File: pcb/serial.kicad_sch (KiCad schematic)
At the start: 13 parts, among them J10 SHIELD, J11 DE9_Pins_MountingHoles, J12 01x09, J13 01x09, U94 MAX232

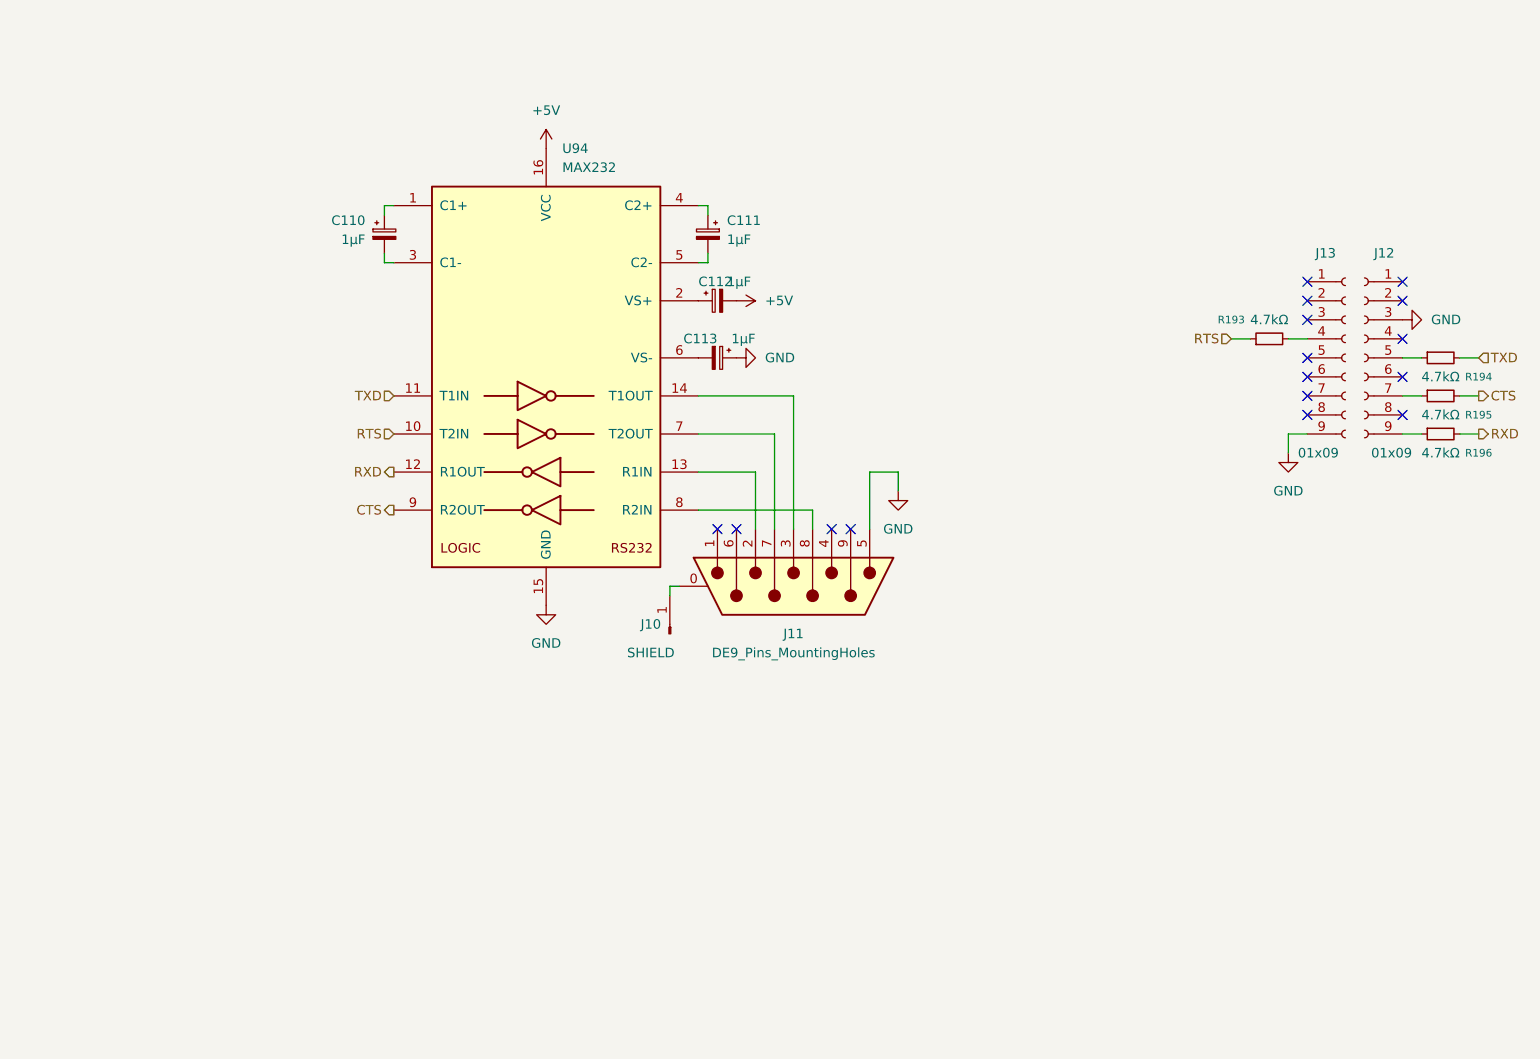
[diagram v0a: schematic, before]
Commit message: WIP PCB (add bypass caps, minor fixes)
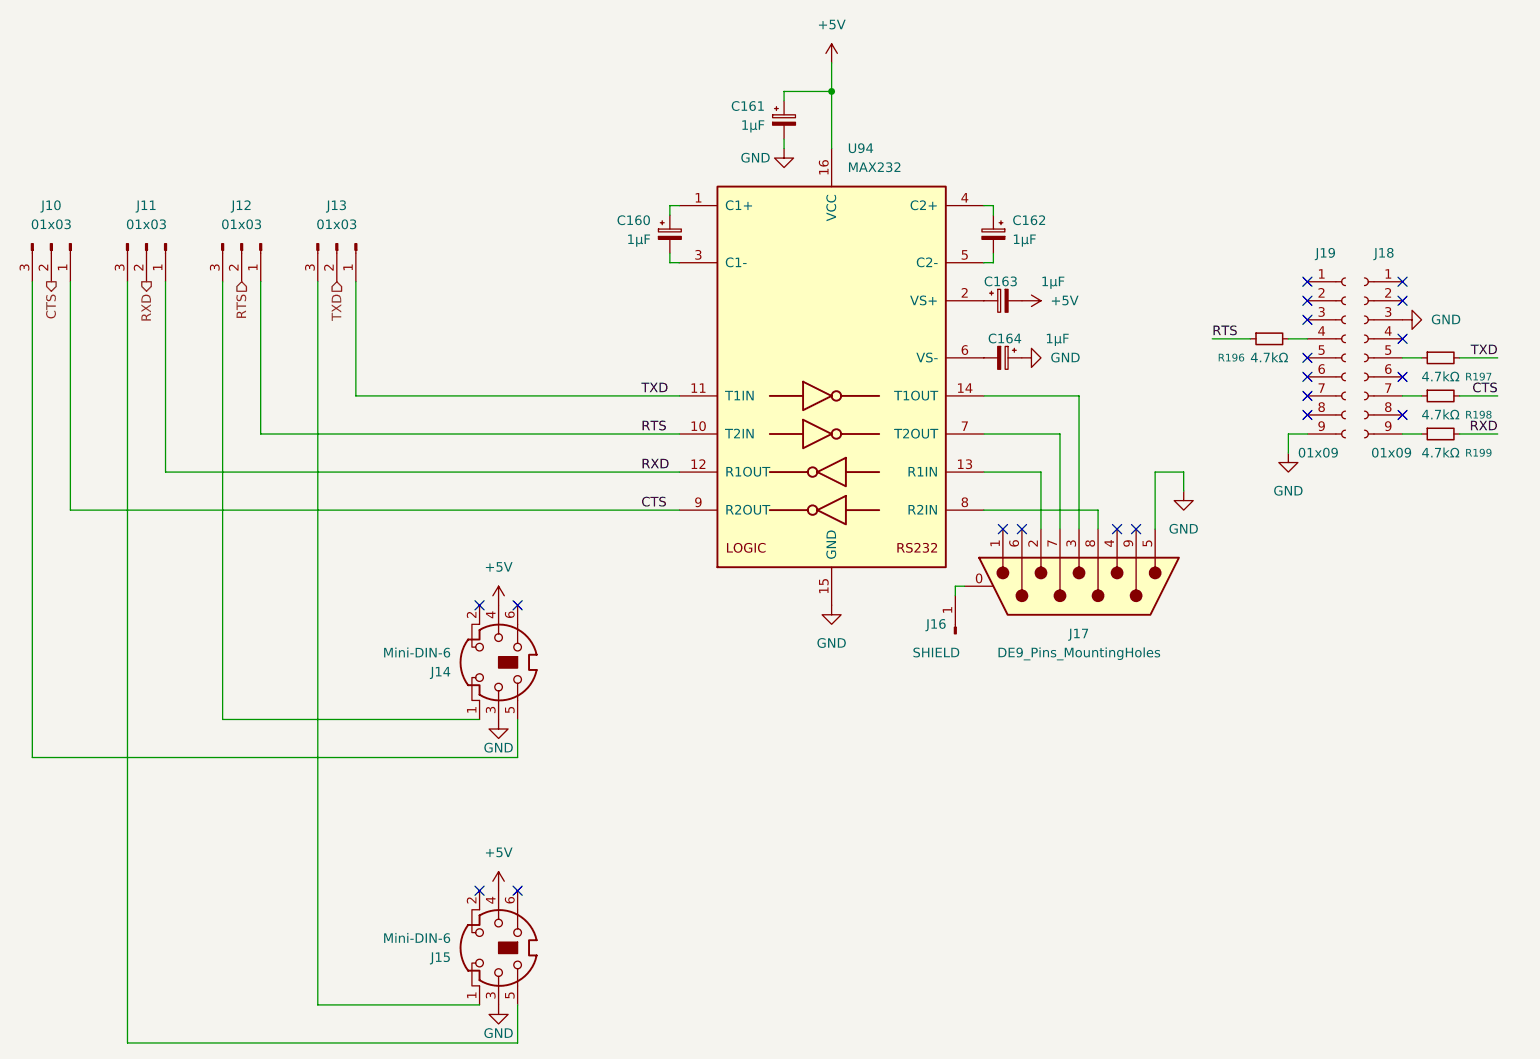
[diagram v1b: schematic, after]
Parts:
- added C161: 1µF, symbol Device:C_Polarized_Small
- added J10, J11, J12, J13: 01x03, symbol Connector:Conn_01x03_Pin
- added J14, J15: Mini-DIN-6, symbol Connector:Mini-DIN-6
- renumbered C110 to C160, C111 to C162, C112 to C163, C113 to C164, J10 to J16, J11 to J17, J12 to J18, J13 to J19, R193 to R196, R194 to R197, R195 to R198, R196 to R199
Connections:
- net +5V: now also C161.1, J14.4, J15.4
- net CTS: now also J10.1 (Pin_1), J10.2 (Pin_2)
- net GND: now also C161.2, J14.3, J15.3
- net RTS: now also J12.1 (Pin_1), J12.2 (Pin_2)
- net RXD: now also J11.1 (Pin_1), J11.2 (Pin_2)
- net TXD: now also J13.1 (Pin_1), J13.2 (Pin_2)
- new net: J12.3 (Pin_3), J14.1
- new net: J10.3 (Pin_3), J14.5
- new net: J13.3 (Pin_3), J15.1
- new net: J11.3 (Pin_3), J15.5
- no-connect marks 16 -> 20
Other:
- moved on the sheet: C160, C162, C163, C164, J16, J17, U94
